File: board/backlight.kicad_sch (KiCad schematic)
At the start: 12 parts, among them U1801 TPS61176

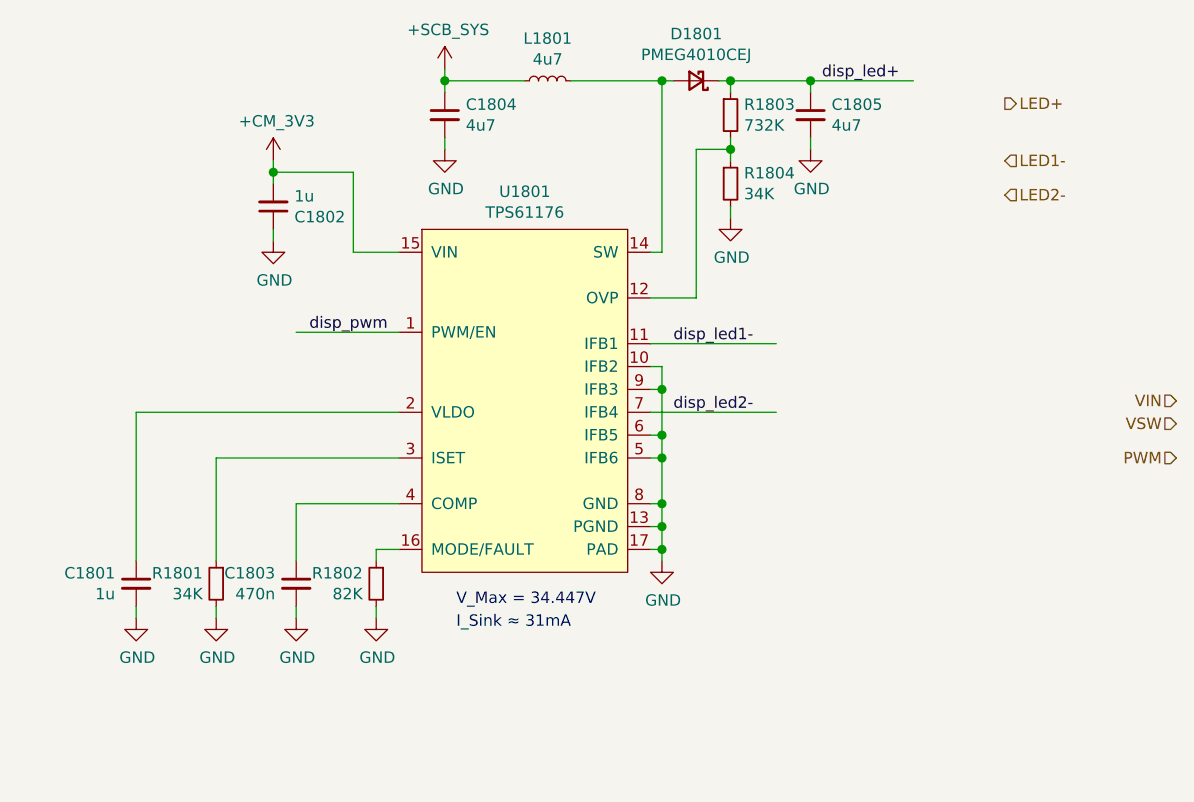
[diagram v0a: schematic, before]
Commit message: Added testpoints and other fixes
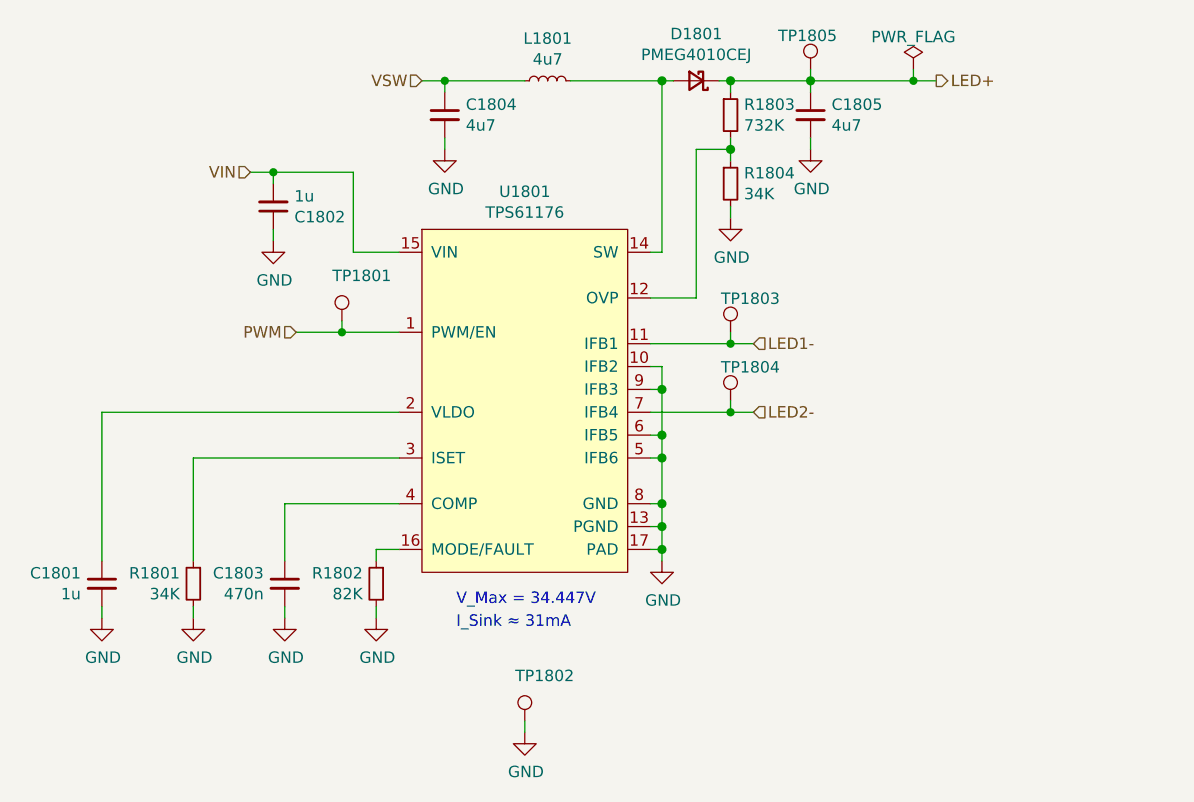
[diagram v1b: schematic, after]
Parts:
- added TP1801, TP1802, TP1803, TP1804, TP1805: TestPoint, DIYPie:TestPoint_Pad_D1.5mm, symbol DIYPie:TestPoint
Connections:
- net +3V3 is gone; now on net VIN: C1802.2, U1801.15 (VIN)
- net +5V is gone; now on net VSW: C1804.1, L1801.1
- net disp_led+ is gone; now on net LED+: C1805.1, D1801.1 (K), R1803.1
- net disp_led1- is gone; now on net LED1-: U1801.11 (IFB1)
- net disp_led2- is gone; now on net LED2-: U1801.7 (IFB4)
- net disp_pwm is gone; now on net PWM: U1801.1 (PWM/EN)
- net GND: now also TP1802.1
- net LED+: now also TP1805.1
- net LED1-: now also TP1803.1
- net LED2-: now also TP1804.1
- net PWM: now also TP1801.1
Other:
- moved on the sheet: C1801, C1803, R1801
